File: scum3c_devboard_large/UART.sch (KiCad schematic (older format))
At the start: 24 parts, among them J2 47346-0001, U2 FT231XS-U, U3 74AVC1T45GS,132, U4 74AVC1T45GS,132, U5 LP5907MFX-1.5

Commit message: ready for merge
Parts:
- removed C12, C8: LED, Capacitor_SMD:C_0402_1005Metric, symbol Device:C
- removed NT1: Net-Tie_2, NetTie:NetTie-2_SMD_Pad0.5mm, symbol Device:Net-Tie_2
- removed R5, R6: NP, Resistor_SMD:R_0402_1005Metric, symbol Device:R_US
- added D1, D2: LED, LED_SMD:LED_0402_1005Metric, symbol Device:LED
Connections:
- net labels added: VBAT_USB
- net labels removed: +VBAT
- wire segments 41 -> 36
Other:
- note added: "Level Shifters"
- note added: "USB"
- note added: "USB to UART"
- note added: "Voltage Regulator"
- note removed: "Populate One. Choose VDDIO = 3.3V or 1.5V"
- moved on the sheet: C1, C10, C11, C2, C3, C4, C5, C6, C7, J2, L1, R1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

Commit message: replaced level shifters and other changes
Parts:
- removed C1, C3: 10uF, Capacitor_SMD:C_0402_1005Metric, symbol Device:C
- removed U5: LP5907MFX-1.5, downloaded_libs:SOT95P280X145-5N, symbol LP5907:LP5907MFX-3.3_NOPB
- added J9: Conn_02x03_Odd_Even, Connector_PinHeader_2.54mm:PinHeader_2x03_P2.54mm_Vertical, symbol Connector_Generic:Conn_02x03_Odd_Even
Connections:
- net labels added: +VBAT, +VIN, RsRx33USB, RsRxTeensy, RsTx33USB, RsTxTeensy
- net labels removed: VBAT_USB
- wire segments 36 -> 28
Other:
- note added: "Jumpers"
- note removed: "Voltage Regulator"
- moved on the sheet: C10, C11, C2, C4, C5, C6, C7, D1, D2, J2, L1, R1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

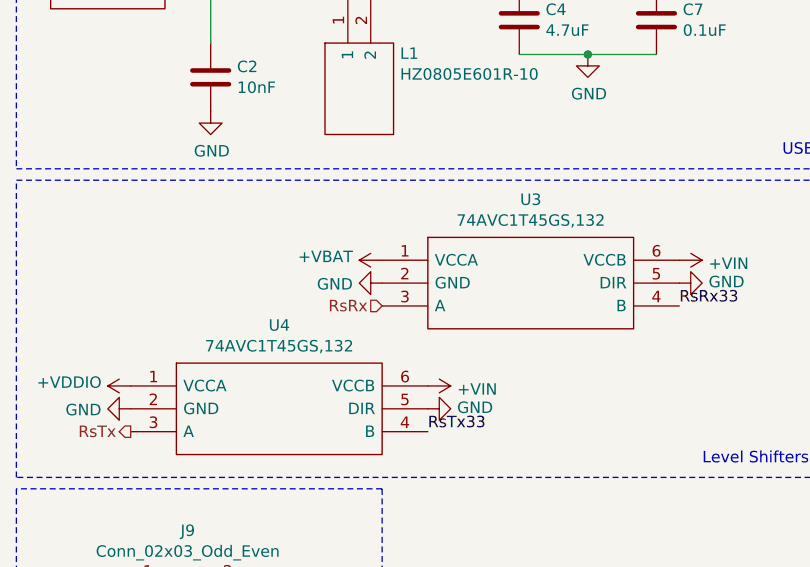
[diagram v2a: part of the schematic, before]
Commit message: With through-hole antenna
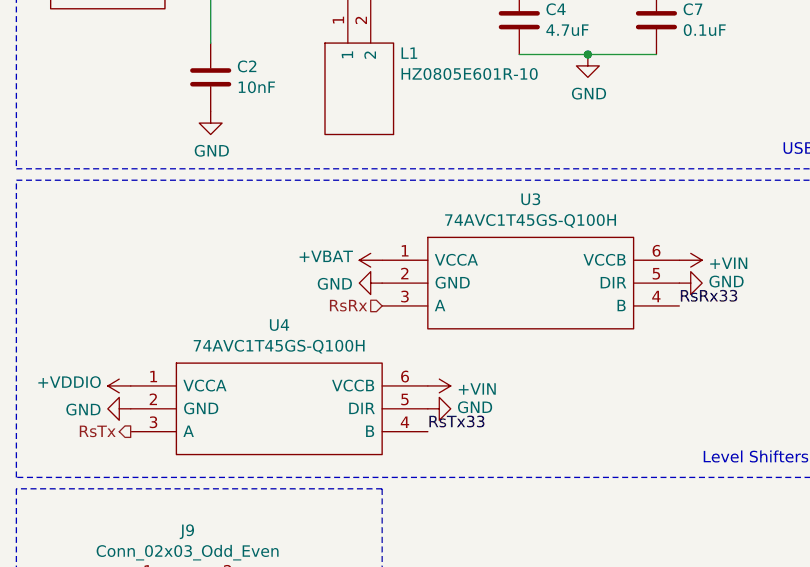
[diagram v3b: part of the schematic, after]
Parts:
- U3, U4: value 74AVC1T45GS,132 -> 74AVC1T45GS-Q100H
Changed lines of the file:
@@
 P 2150 5050
 F 0 "U3" H 2800 5315 50  0000 C CNN
-F 1 "74AVC1T45GS,132" H 2800 5224 50  0000 C CNN
+F 1 "74AVC1T45GS-Q100H" H 2800 5224 50  0000 C CNN
 F 2 "SamacSys_Parts:74LVC1G3157GS132" H 3300 5150 50  0001 L CNN
 F 3 "https://assets.nexperia.com/documents/data-sheet/74AVC1T45.pdf" H 3300 5050 50  0001 L CNN
@@
 P 1050 5600
 F 0 "U4" H 1700 5865 50  0000 C CNN
-F 1 "74AVC1T45GS,132" H 1700 5774 50  0000 C CNN
+F 1 "74AVC1T45GS-Q100H" H 1700 5774 50  0000 C CNN
 F 2 "SamacSys_Parts:74LVC1G3157GS132" H 2200 5700 50  0001 L CNN
 F 3 "https://assets.nexperia.com/documents/data-sheet/74AVC1T45.pdf" H 2200 5600 50  0001 L CNN

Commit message: Suggested changes
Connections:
- net +VDDIO: now also U4.5 (DIR)
- net GND: no longer U4.5 (DIR)
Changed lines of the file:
@@
 EESchema Schematic File Version 4
 LIBS:scum3c-devboard-cache
-EELAYER 26 0
+EELAYER 30 0
 EELAYER END
 $Descr A4 11693 8268
 encoding utf-8
-Sheet 3 4
+Sheet 2 4
 Title ""
 Date ""
@@
 NoConn ~ 2000 1950
 $Comp
-L draft1library:+UART33 #PWR0110
+L SCUM:+UART33 #PWR0110
 U 1 1 5F3A76F2
 P 1400 2500
@@
 D_N
 $Comp
-L draft1library:+UART33 #PWR0120
+L SCUM:+UART33 #PWR0120
 U 1 1 5F3BAA75
 P 3300 1750
@@
 $EndComp
 $Comp
-L draft1library:+UART33 #PWR0122
+L SCUM:+UART33 #PWR0122
 U 1 1 5F3BDA8D
 P 3900 750
@@
 	1250 2900 1250 2300
 $Comp
-L draft1library:+UART33 #PWR0124
+L SCUM:+UART33 #PWR0124
 U 1 1 5F3A0BD3
 P 1250 1350
@@
 Wire Wire Line
 	1250 1350 2000 1350
-Connection ~ 1250 1350
 $Comp
 L SamacSys_Parts:47346-0001 J2
@@
 $EndComp
 $Comp
-L draft1library:+VUSB #PWR0127
+L SCUM:+VUSB #PWR0127
 U 1 1 5F3E9DCE
 P 3050 3850
@@
 Wire Wire Line
 	2100 3850 2750 3850
-Wire Wire Line
-	2750 3850 3050 3850
 Connection ~ 2750 3850
-Wire Wire Line
-	3050 3850 3350 3850
-Connection ~ 3050 3850
-$Comp
-L draft1library:+VUSB #PWR0146
+$Comp
+L SCUM:+VUSB #PWR0146
 U 1 1 5F3B5939
 P 3300 1650
@@
 Level Shifters
 $Comp
-L draft1library:+VBAT #PWR0129
+L SCUM:+VBAT #PWR0129
 U 1 1 60087316
 P 2150 5050
@@
 F 3 "" H 2150 5050 50  0001 C CNN
 	1    2150 5050
-	0    -1   -1   0
-$EndComp
-$Comp
-L power:GND #PWR0136
-U 1 1 6008930D
-P 2350 5700
-F 0 "#PWR0136" H 2350 5450 50  0001 C CNN
-F 1 "GND" V 2355 5572 50  0000 R CNN
-F 2 "" H 2350 5700 50  0001 C CNN
-F 3 "" H 2350 5700 50  0001 C CNN
-	1    2350 5700
 	0    -1   -1   0
 $EndComp
@@
 	2150 6050 550  6050
 $Comp
-L draft1library:+VIN #PWR0145
+L SCUM:+VIN #PWR0145
 U 1 1 6009C881
 P 3450 5050
@@
 $EndComp
 $Comp
-L draft1library:+VIN #PWR0149
+L SCUM:+VIN #PWR0149
 U 1 1 6009C8CC
 P 2350 5600
@@
 $EndComp
 $Comp
-L draft1library:+VDDIO #PWR0191
+L SCUM:+VDDIO #PWR0191
 U 1 1 600C2506
 P 1050 5600
@@
 	0    -1   -1   0
 $EndComp
+$Comp
+L SCUM:+VDDIO #PWR0136
+U 1 1 6074166E
+P 2350 5700
+F 0 "#PWR0136" H 2350 5550 50  0001 C CNN
+F 1 "+VDDIO" V 2350 5800 50  0000 L CNN
+F 2 "" H 2350 5700 50  0001 C CNN
+F 3 "" H 2350 5700 50  0001 C CNN
+	1    2350 5700
+	0    1    1    0
+$EndComp
+Wire Wire Line
+	2750 3850 3050 3850
+Connection ~ 3050 3850
+Wire Wire Line
+	3050 3850 3350 3850
 $EndSCHEMATC

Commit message: switching computers
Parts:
- removed J2: 47346-0001, Connector_USB:USB_Micro-B_Molex_47346-0001, symbol SamacSys_Parts:47346-0001
- added C13: C, symbol Device:C
- added J5: 1050170001, SCUM:MOLEX_1050170001, symbol SCUM:1050170001
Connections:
- net D_N: now also J5.2
- net D_P: now also J5.3
- net GND: now also C13.2, J5.5
- net at U2.10 (CBUS2): now also D1.1 (K); no longer D1.2 (A)
- net at U2.17 (CBUS1): now also D2.1 (K); no longer D2.2 (A)
- net at R4.2: now also D2.2 (A); no longer D2.1 (K)
- net at R1.2: now also D1.2 (A); no longer D1.1 (K)
- net at C2.1, L1.1: now also J5.1
- net +UART33 renamed +USB33
- new net: C13.1, J5.SH1 (SHIELD), J5.SH2 (SHIELD), J5.SH3 (SHIELD), J5.SH4 (SHIELD), J5.SH5 (SHIELD), J5.SH6 (SHIELD), J5.SH7 (SHIELD), J5.SH8 (SHIELD)
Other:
- note added: "UART Level Shifters"
- note removed: "Level Shifters"
- moved on the sheet: C2, C4, C7, D1, D2, L1

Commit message: ready for review
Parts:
- C13: footprint (none) -> Capacitor_SMD:C_0402_1005Metric
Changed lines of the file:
@@
 EESchema Schematic File Version 4
 LIBS:scum3c-devboard-cache
-EELAYER 30 0
+EELAYER 26 0
 EELAYER END
 $Descr A4 11693 8268
@@
 F 0 "C13" H 1365 4296 50  0000 L CNN
 F 1 "C" H 1365 4205 50  0000 L CNN
-F 2 "" H 1288 4100 50  0001 C CNN
+F 2 "Capacitor_SMD:C_0402_1005Metric" H 1288 4100 50  0001 C CNN
 F 3 "~" H 1250 4250 50  0001 C CNN
 	1    1250 4250
